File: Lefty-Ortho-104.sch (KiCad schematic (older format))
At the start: 18 parts

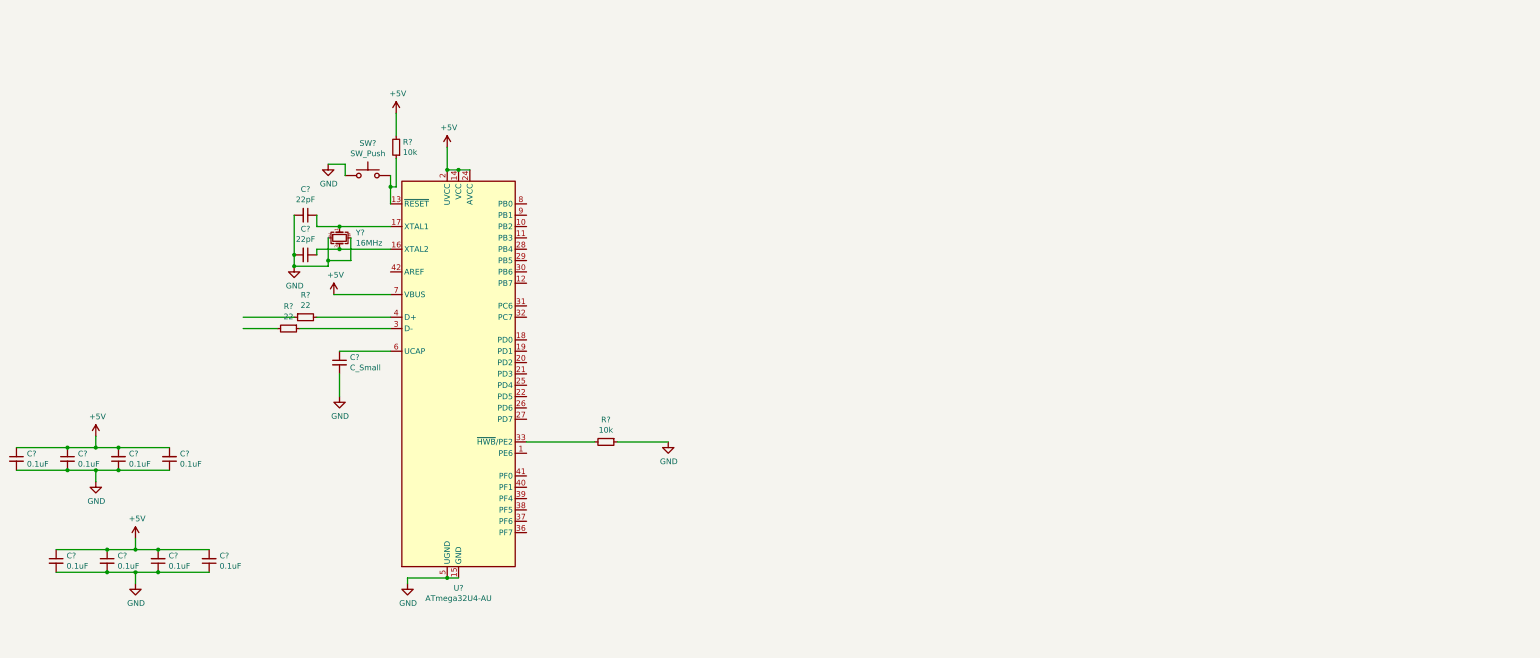
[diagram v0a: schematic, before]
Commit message: update to kicad 8
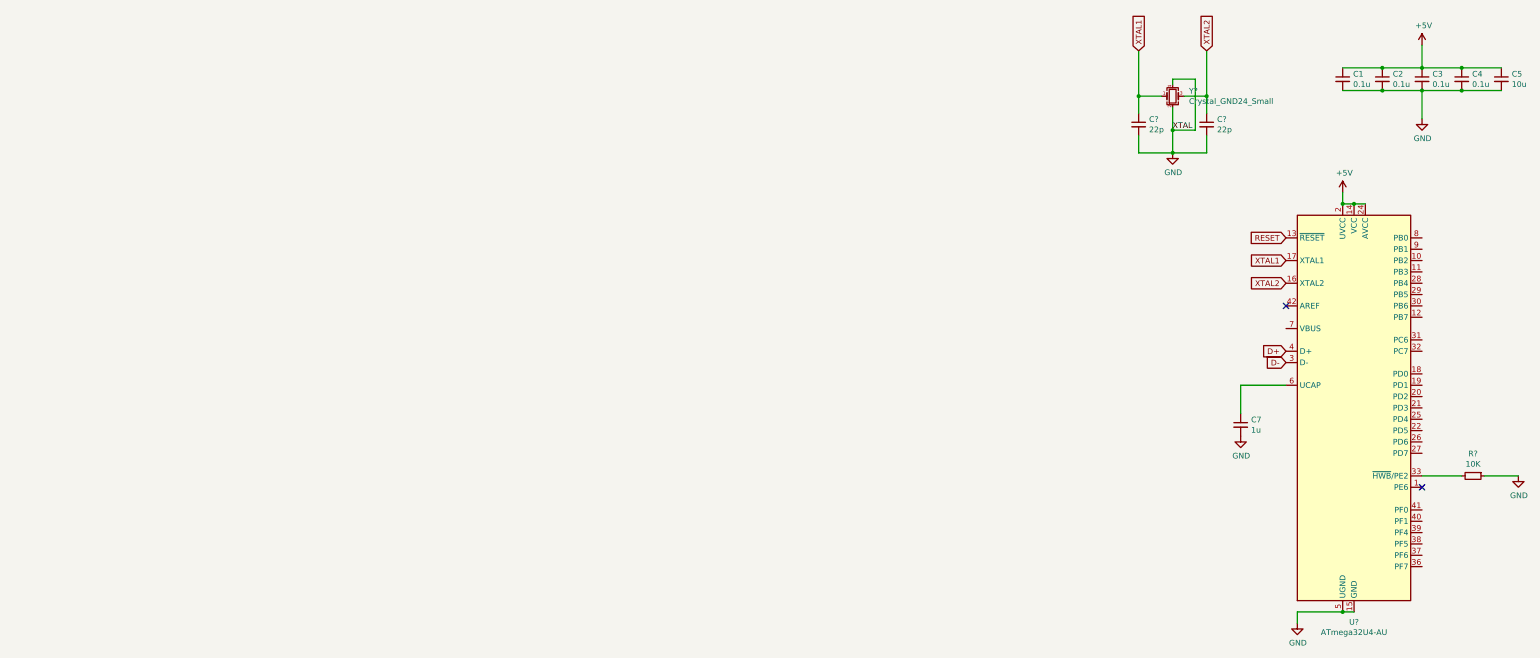
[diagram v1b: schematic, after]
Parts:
- removed C?: C_Small, symbol Device:C_Small
- removed C? (x8): 0.1uF, symbol Device:C_Small
- removed C? (x2): 22pF, symbol Device:C_Small
- removed R? (x2): 10k, symbol Device:R_Small
- removed R? (x2): 22, symbol Device:R_Small
- removed SW?: SW_Push, symbol Switch:SW_Push
- removed U?: ATmega32U4-AU, Package_QFP:TQFP-44_10x10mm_P0.8mm, symbol MCU_Microchip_ATmega:ATmega32U4-AU
- removed Y?: 16MHz, symbol Device:Crystal_GND24_Small
- added C1, C2, C3, C4: 0.1u, symbol Device:C_Small
- added C5: 10u, symbol Device:C_Small
- added C7: 1u, symbol Device:C_Small
- added C? (x2): 22p, symbol Device:C_Small
- added R?: 10K, symbol Device:R_Small
- added U?: ATmega32U4-AU, Package_QFP:TQFP-44_10x10mm_P0.8mm, symbol MCU_Microchip_ATmega:ATmega32U4-AU
- added Y?: Crystal_GND24_Small, symbol Device:Crystal_GND24_Small
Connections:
- net labels added: D+, D-, RESET, XTAL, XTAL1, XTAL2
- wire segments 55 -> 36
- no-connect marks 0 -> 2
